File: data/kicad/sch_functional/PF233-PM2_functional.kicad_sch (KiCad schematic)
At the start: 17 parts, among them J1 MT60-M leads: BAT+ BAT- ILK, J3 Power switch pair (top housin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, Q1 Si4401FDY -40V

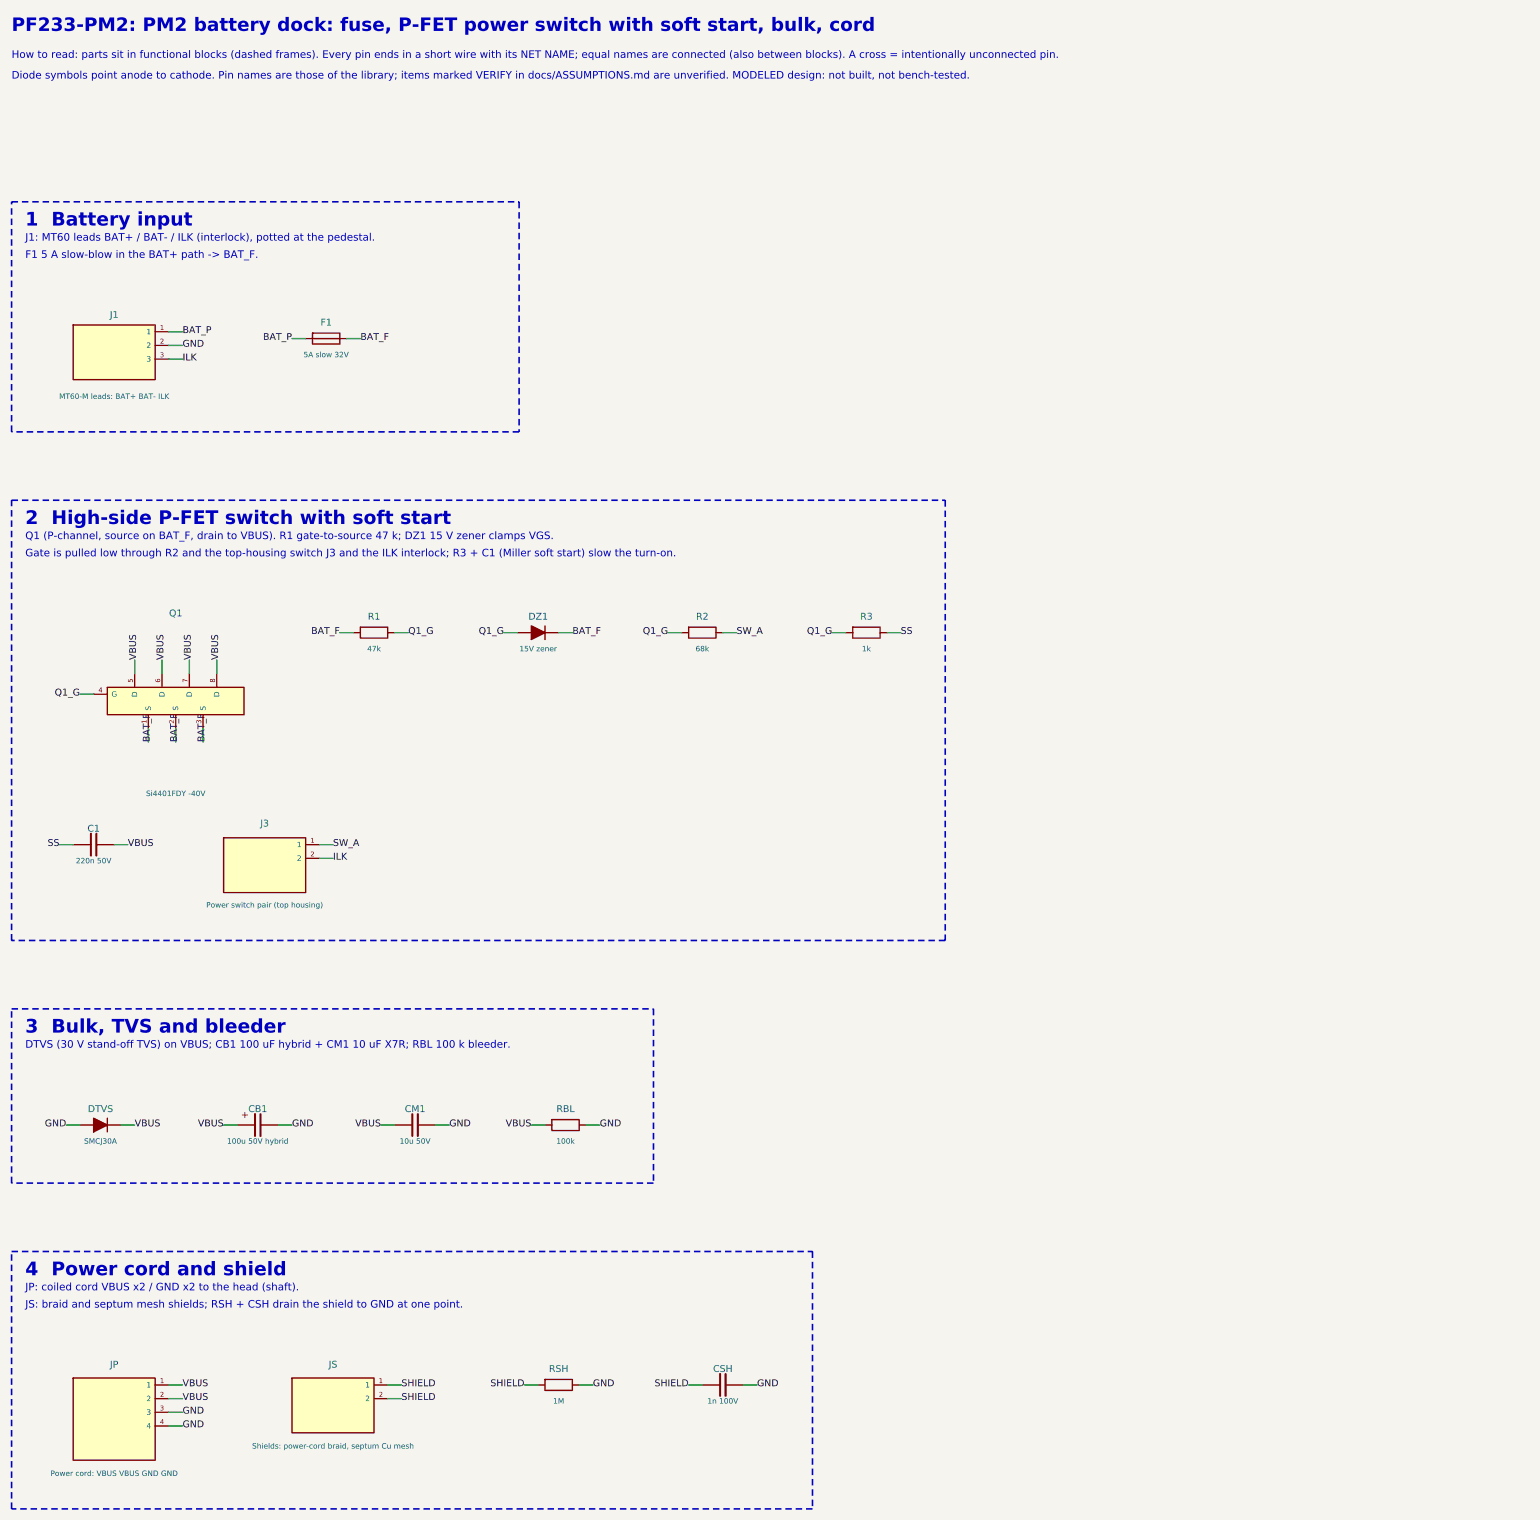
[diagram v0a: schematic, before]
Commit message: WIP (NOT signed off): data published by the first close-out sign-off run, which had 5 FAIL (CB1D-C2 / AU1 fine-pitch clearance); superseded by the rerun in progress
Co-Authored-By: Claude Opus 5.5 <noreply@anthropic.com>
Claude-Session: https://claude.ai/code/session_01FX4DWSYYjMCFGGA6gmha65
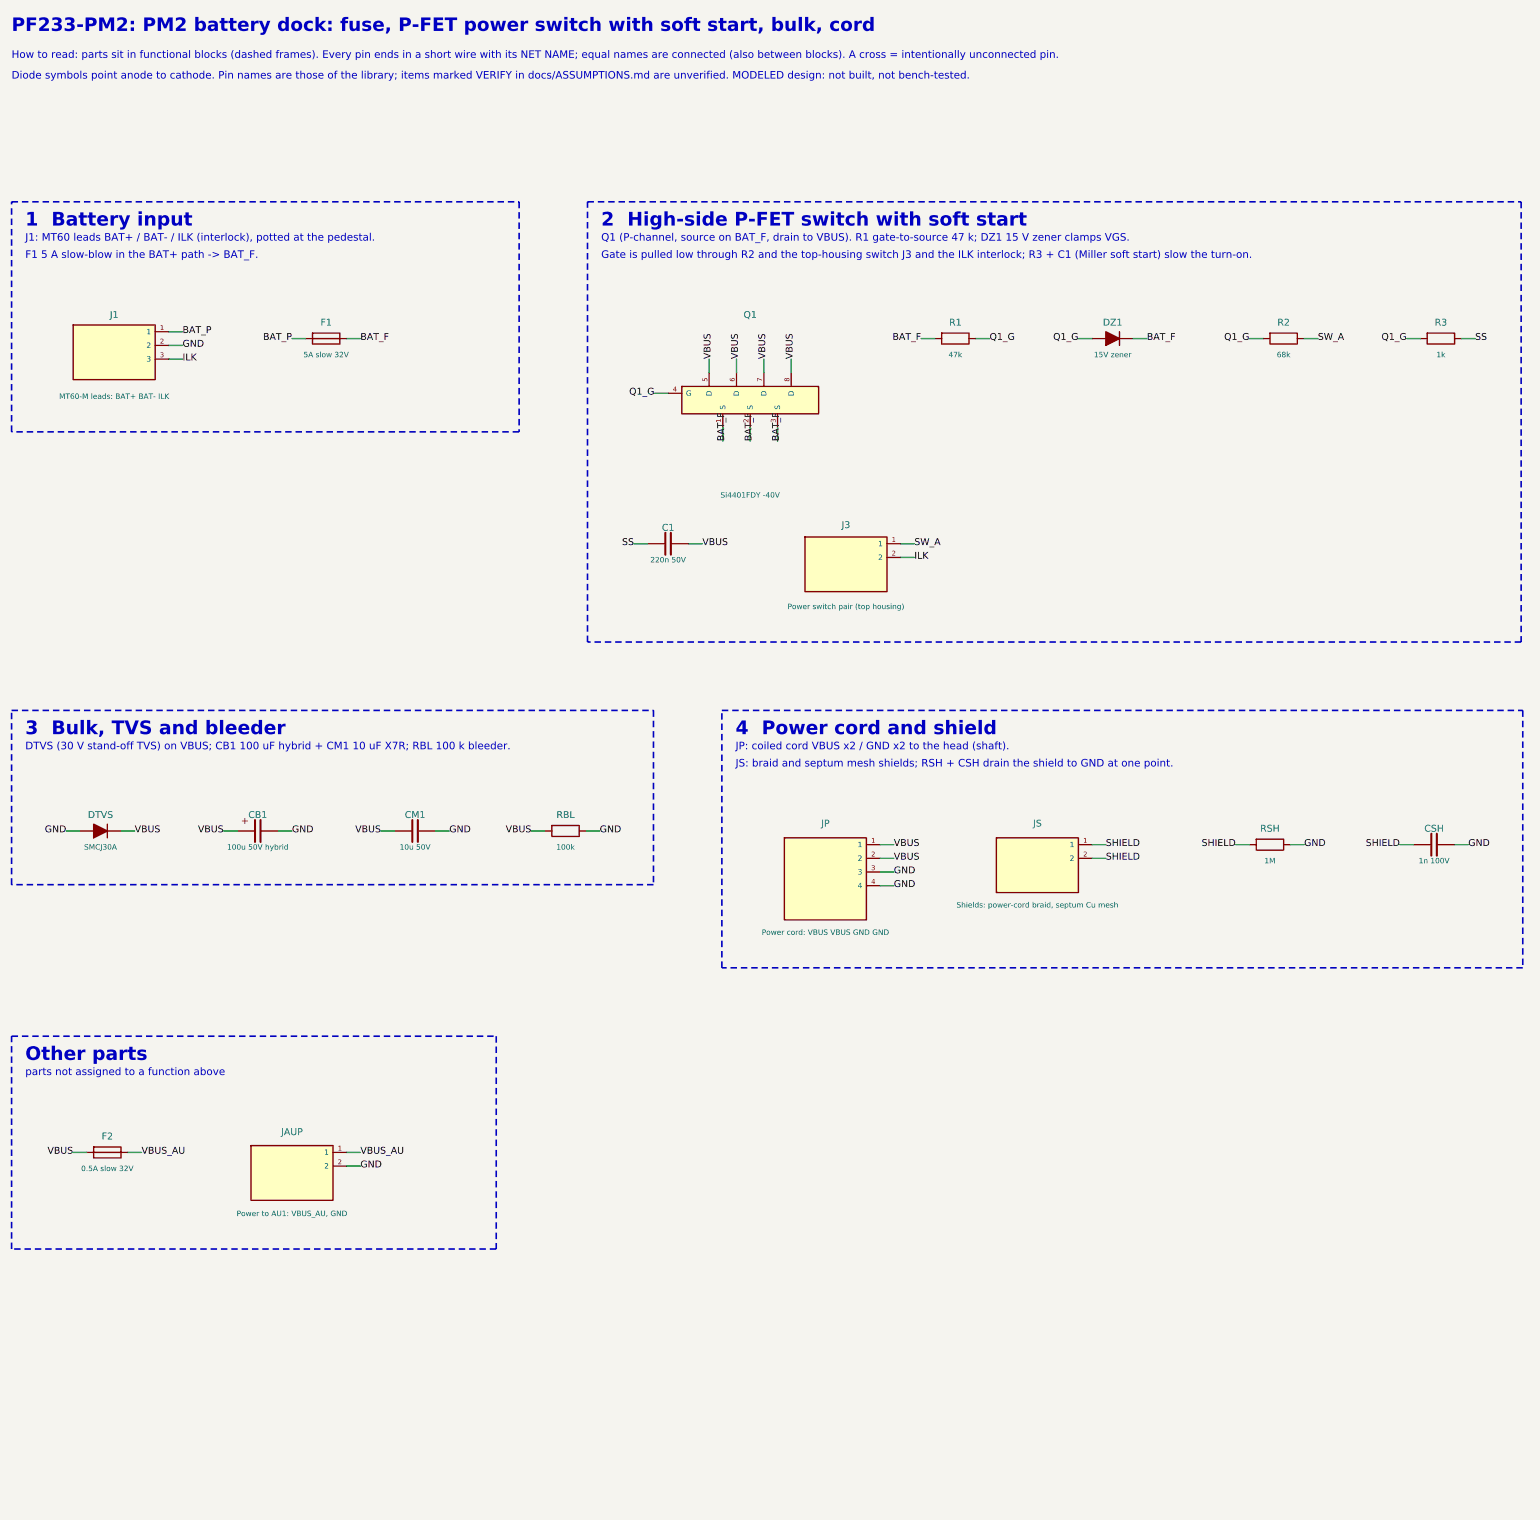
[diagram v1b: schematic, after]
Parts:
- added F2: 0.5A slow 32V, Fuse:Fuse_1206_3216Metric, symbol PF233F:F_H
- added JAUP: Power to AU1: VBUS_AU, GND, Connector:SolderPad_2x_P5.08mm, symbol PF233F:BOX_WIRE2
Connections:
- net GND: now also JAUP.2
- net VBUS: now also F2.1
- new net VBUS_AU: F2.2, JAUP.1
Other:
- note added: "Other parts"
- note added: "parts not assigned to a function above"
- moved on the sheet: C1, CB1, CM1, CSH, DTVS, DZ1, J3, JP, JS, Q1, R1, R2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
